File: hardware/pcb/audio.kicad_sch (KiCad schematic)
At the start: 18 parts, among them IC3 TAC5212, J4 PJ-342, J5 PJ-242

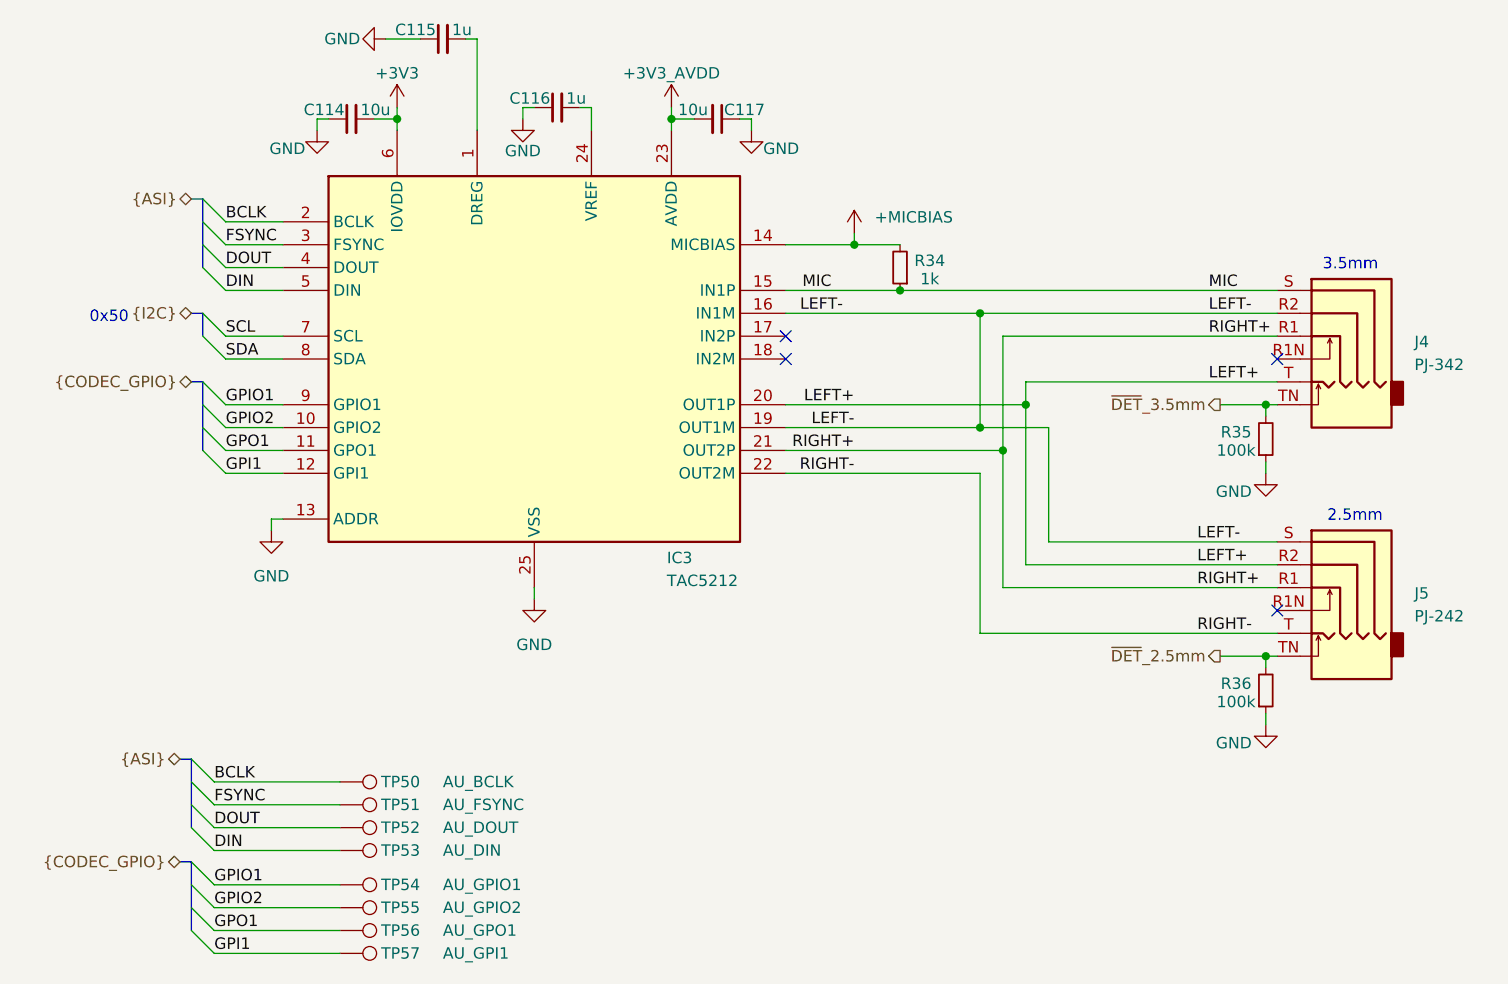
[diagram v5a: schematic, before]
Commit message: added pullups for jtag
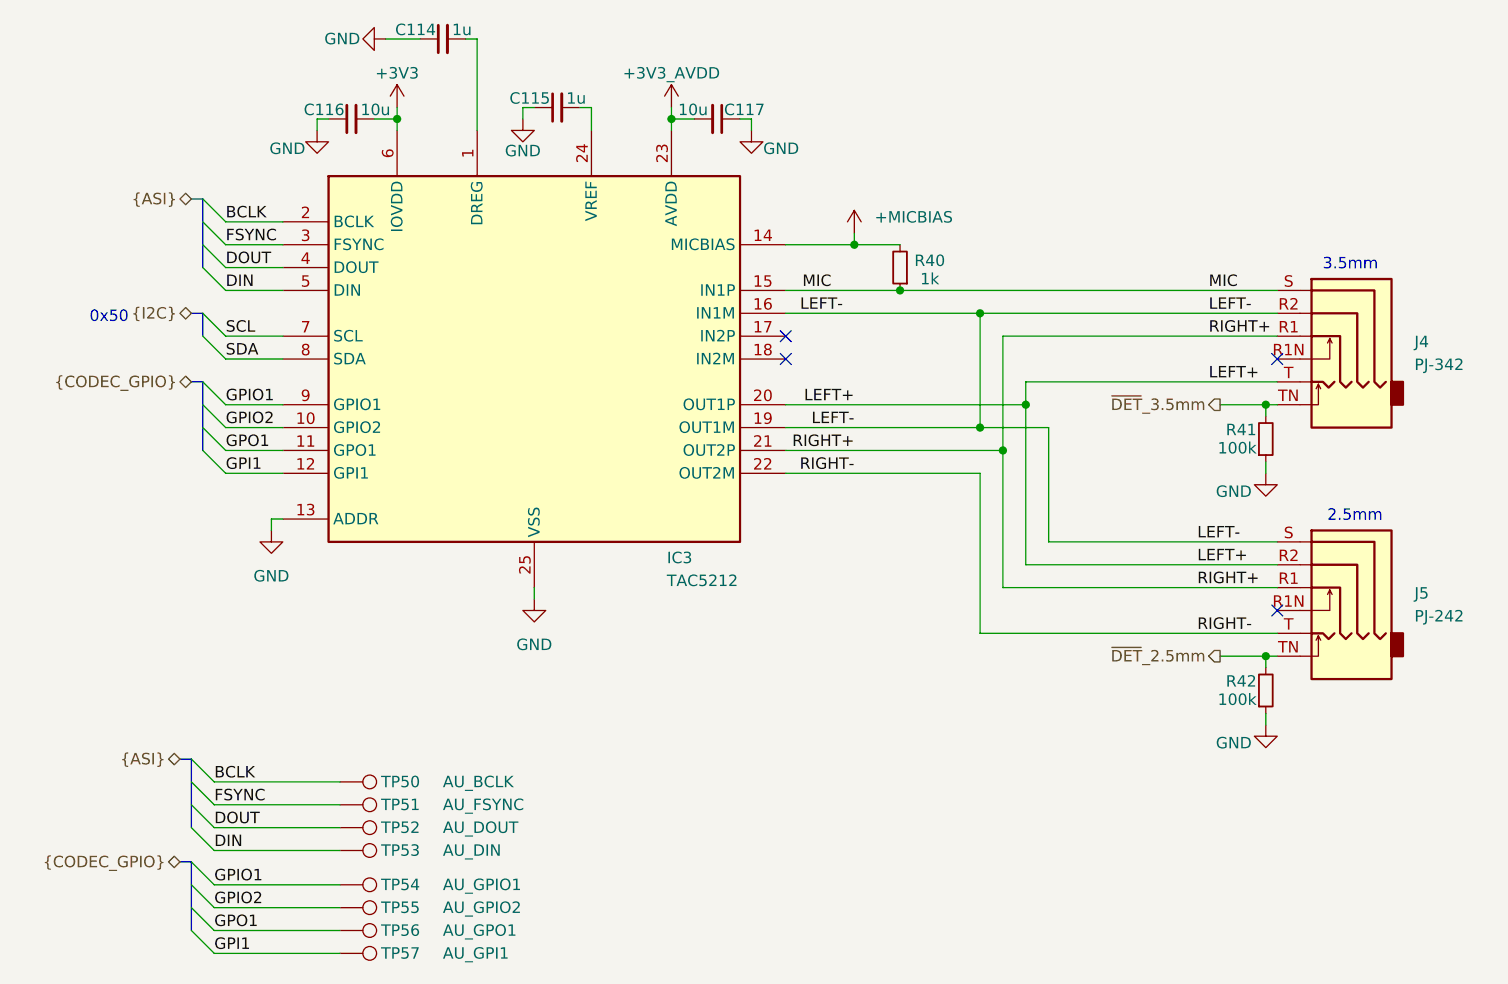
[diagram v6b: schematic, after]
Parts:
- removed R36: 100k, Resistor_SMD:R_0402_1005Metric, symbol Device:R_Small
- added R42: 100k, Resistor_SMD:R_0402_1005Metric, symbol Device:R_Small
- renumbered C115 to C114, C116 to C115, C114 to C116, R34 to R40, R35 to R41
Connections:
- net GND: now also R42.1
- net ~{DET}_2.5mm: now also R42.2

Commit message: vendored in a bunch of footprints
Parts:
- J4: footprint PCM_ckl-connector:Jack_3.5mm_SHOUHAN_PJ-342 -> ckl:Jack_3.5mm_SHOUHAN_PJ-342
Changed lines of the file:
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@@
 			)
 		)
-		(property "Footprint" "PCM_ckl-connector:Jack_3.5mm_SHOUHAN_PJ-342"
+		(property "Footprint" "ckl:Jack_3.5mm_SHOUHAN_PJ-342"
 			(at 162.56 54.61 0)
 			(hide yes)

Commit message: changed stackup, creted tuning profiles, created net classes
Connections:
- net GND: no longer IC3.26 (VSS), IC3.27 (VSS), IC3.28 (VSS), IC3.29 (VSS)
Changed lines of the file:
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@@
 		(pin "19"
-		)
-		(pin "28"
 		)
 		(pin "13"
 		)
 		(pin "14"
-		)
-		(pin "26"
 		)
 		(pin "7"
@@
 		(pin "15"
 		)
-		(pin "29"
-		)
-		(pin "27"
-		)
 		(pin "24"
